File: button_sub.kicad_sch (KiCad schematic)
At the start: 6 parts, among them U3 LTV-817M

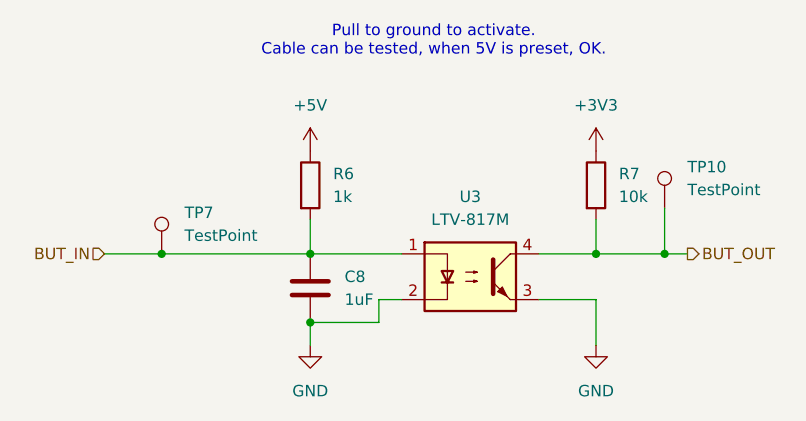
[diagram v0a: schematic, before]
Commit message: Place opto couplers and some connectors.
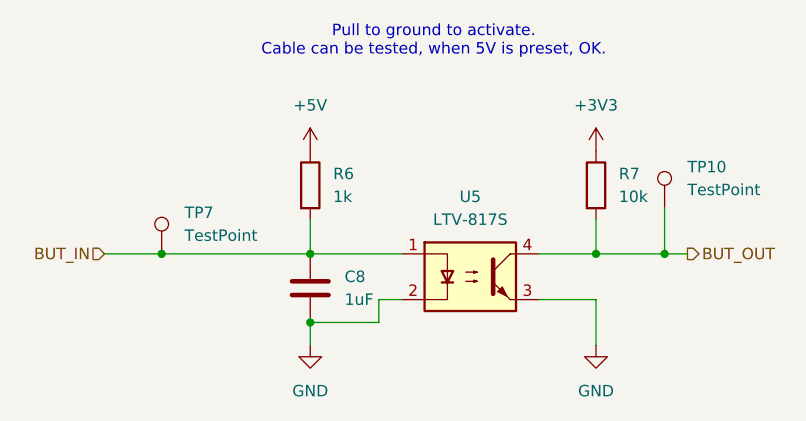
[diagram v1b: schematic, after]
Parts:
- removed U3: LTV-817M, Package_DIP:DIP-4_W10.16mm, symbol Isolator:LTV-817M
- added U5: LTV-817S, Package_DIP:SMDIP-4_W9.53mm, symbol Isolator:LTV-817S
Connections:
- net BUT_IN: now also U5.1
- net BUT_OUT: now also U5.4
- net GND: now also U5.2, U5.3
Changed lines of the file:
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@@
+	)
+	(symbol
+		(lib_id "Isolator:LTV-817S")
+		(at 151.13 99.06 0)
+		(unit 1)
+		(exclude_from_sim no)
+		(in_bom yes)
+		(on_board yes)
+		(dnp no)
+		(fields_autoplaced yes)
+		(property "Reference" "U5"
+			(at 151.13 90.17 0)
+			(effects
+				(font
+					(size 1.27 1.27)
+				)
+			)
+		)
+		(property "Value" "LTV-817S"
+			(at 151.13 92.71 0)
+			(effects
+				(font
+					(size 1.27 1.27)
+				)
+			)
+		)
+		(property "Footprint" "Package_DIP:SMDIP-4_W9.53mm"
+			(at 151.13 106.68 0)
+			(effects
+				(font
+					(size 1.27 1.27)
+				)
+				(hide yes)
+			)
+		)
+		(property "Datasheet" "https://www.lcsc.com/product-detail/C109227.html"
+			(at 142.24 91.44 0)
+			(effects
+				(font
+					(size 1.27 1.27)
+				)
+				(hide yes)
+			)
+		)
+		(property "Description" "DC Optocoupler, Vce 35V, CTR 50%, SMDIP-4"
+			(at 151.13 99.06 0)
+			(effects
+				(font
+					(size 1.27 1.27)
+				)
+				(hide yes)
+			)
+		)
+		(property "LCSC" "C109227"
+			(at 151.13 99.06 0)
+			(effects
+				(font
+					(size 1.27 1.27)
+				)
+				(hide yes)
+			)
+		)
+		(pin "4"
+		)
+		(pin "2"
+		)
+		(pin "3"
+		)
+		(pin "1"
+		)
+		(instances
+			(project ""
+				(path "/4ab90003-ea4c-4878-8117-f834ac24f8d9/2279bf67-9a91-44f0-b5c7-36e7b6560aca/1b213c25-d2ee-4039-b440-713ca9411fa9"
+					(reference "U5")
+					(unit 1)
+				)
+				(path "/4ab90003-ea4c-4878-8117-f834ac24f8d9/2279bf67-9a91-44f0-b5c7-36e7b6560aca/966e223a-98da-4719-87d2-fe9fc7de1219"
+					(reference "U6")
+					(unit 1)
+				)
+				(path "/4ab90003-ea4c-4878-8117-f834ac24f8d9/2279bf67-9a91-44f0-b5c7-36e7b6560aca/fcd7be72-9c9e-4717-8056-7ec02dc0e81d"
+					(reference "U7")
+					(unit 1)
+				)
+			)
+		)
 	)
 	(symbol
@@
 					(unit 1)
 				)
-			)
-		)
-	)
-	(symbol
-		(lib_id "Isolator:LTV-817M")
-		(at 151.13 99.06 0)
-		(unit 1)
-		(exclude_from_sim no)
-		(in_bom yes)
-		(on_board yes)
-		(dnp no)
-		(fields_autoplaced yes)
-		(property "Reference" "U3"
-			(at 151.13 90.17 0)
-			(effects
-				(font
-					(size 1.27 1.27)
-				)
-			)
-		)
-		(property "Value" "LTV-817M"
-			(at 151.13 92.71 0)
-			(effects
-				(font
-					(size 1.27 1.27)
-				)
-			)
-		)
-		(property "Footprint" "Package_DIP:DIP-4_W10.16mm"
-			(at 151.13 106.68 0)
-			(effects
-				(font
-					(size 1.27 1.27)
-				)
-				(hide yes)
-			)
-		)
-		(property "Datasheet" "https://jlcpcb.com/partdetail/LiteOn-LTV_817S_TA1C/C109227"
-			(at 140.97 91.44 0)
-			(effects
-				(font
-					(size 1.27 1.27)
-				)
-				(hide yes)
-			)
-		)
-		(property "Description" "DC Optocoupler, Vce 35V, CTR 50%, DIP-4"
-			(at 151.13 99.06 0)
-			(effects
-				(font
-					(size 1.27 1.27)
-				)
-				(hide yes)
-			)
-		)
-		(property "LCSC" "C109227"
-			(at 151.13 99.06 0)
-			(effects
-				(font
-					(size 1.27 1.27)
-				)
-				(hide yes)
-			)
-		)
-		(pin "4"
-		)
-		(pin "2"
-		)
-		(pin "3"
-		)
-		(pin "1"
-		)
-		(instances
-			(project "stopnu-hardware"
-				(path "/4ab90003-ea4c-4878-8117-f834ac24f8d9/2279bf67-9a91-44f0-b5c7-36e7b6560aca/1b213c25-d2ee-4039-b440-713ca9411fa9"
-					(reference "U3")
-					(unit 1)
-				)
-				(path "/4ab90003-ea4c-4878-8117-f834ac24f8d9/2279bf67-9a91-44f0-b5c7-36e7b6560aca/966e223a-98da-4719-87d2-fe9fc7de1219"
-					(reference "U4")
-					(unit 1)
-				)
-				(path "/4ab90003-ea4c-4878-8117-f834ac24f8d9/2279bf67-9a91-44f0-b5c7-36e7b6560aca/fcd7be72-9c9e-4717-8056-7ec02dc0e81d"
-					(reference "U2")
-					(unit 1)
-				)

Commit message: Labeled expansion port, fixed en pin U19 (high)
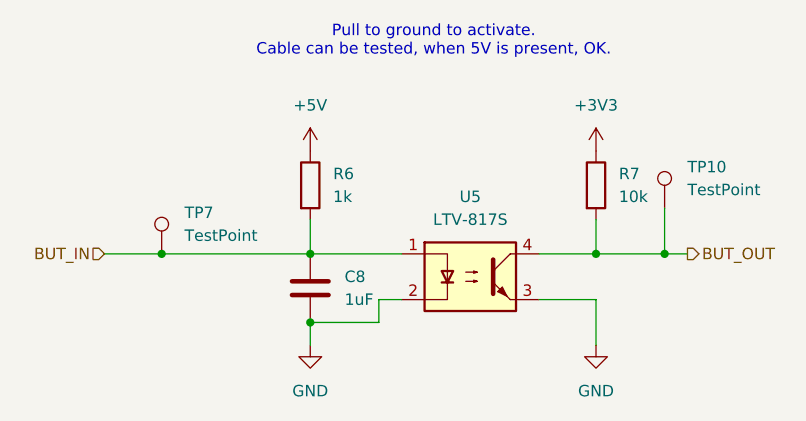
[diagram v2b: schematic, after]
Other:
- note added: "Pull to ground to activate. Cable can be tested, when 5V is present, OK."
- note removed: "Pull to ground to activate. Cable can be tested, when 5V is preset, OK."
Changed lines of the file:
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@@
 	(generator_version "9.0")
 	(paper "A4")
-	(text "Pull to ground to activate.\nCable can be tested, when 5V is preset, OK."
+	(text "Pull to ground to activate.\nCable can be tested, when 5V is present, OK."
 		(exclude_from_sim no)
 		(at 147.066 72.898 0)

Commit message: Add README.md, make power input more intuitive in schematic.
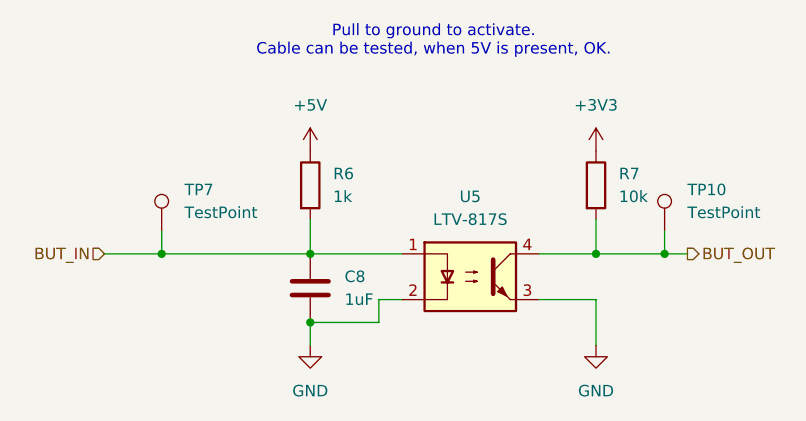
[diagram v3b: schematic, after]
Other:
- moved on the sheet: TP10, TP7
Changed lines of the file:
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@@
+	(wire
+		(pts
+			(xy 116.84 93.98) (xy 116.84 96.52)
+		)
+		(stroke
+			(width 0)
+			(type default)
+		)
+	)
 	(wire
 		(pts
@@
 	(wire
 		(pts
-			(xy 172.72 91.44) (xy 172.72 96.52)
-		)
-		(stroke
-			(width 0)
-			(type default)
-		)
-	)
-	(wire
-		(pts
 			(xy 133.35 96.52) (xy 143.51 96.52)
 		)
@@
 		(pts
 			(xy 133.35 104.14) (xy 133.35 106.68)
+		)
+		(stroke
+			(width 0)
+			(type default)
+		)
+	)
+	(wire
+		(pts
+			(xy 172.72 93.98) (xy 172.72 96.52)
 		)
 		(stroke
@@
 	(symbol
 		(lib_id "Connector:TestPoint")
-		(at 116.84 96.52 0)
+		(at 116.84 93.98 0)
 		(unit 1)
 		(exclude_from_sim no)
@@
 		(fields_autoplaced yes)
 		(property "Reference" "TP7"
+			(at 119.38 89.4079 0)
+			(effects
+				(font
+					(size 1.27 1.27)
+				)
+				(justify left)
+			)
+		)
+		(property "Value" "TestPoint"
 			(at 119.38 91.9479 0)
 			(effects
@@
 			)
 		)
-		(property "Value" "TestPoint"
-			(at 119.38 94.4879 0)
-			(effects
-				(font
-					(size 1.27 1.27)
-				)
-				(justify left)
-			)
-		)
 		(property "Footprint" "TestPoint:TestPoint_Pad_D1.0mm"
-			(at 121.92 96.52 0)
+			(at 121.92 93.98 0)
 			(effects
 				(font
@@
 		)
 		(property "Datasheet" "~"
-			(at 121.92 96.52 0)
+			(at 121.92 93.98 0)
 			(effects
 				(font
@@
 		)
 		(property "Description" "test point"
-			(at 116.84 96.52 0)
+			(at 116.84 93.98 0)
 			(effects
 				(font
@@
 	(symbol
 		(lib_id "Connector:TestPoint")
-		(at 172.72 91.44 0)
+		(at 172.72 93.98 0)
 		(unit 1)
 		(exclude_from_sim no)
@@
 		(fields_autoplaced yes)
 		(property "Reference" "TP10"
-			(at 175.26 86.8679 0)
+			(at 175.26 89.4079 0)
 			(effects
 				(font
@@
 		)
 		(property "Value" "TestPoint"
-			(at 175.26 89.4079 0)
+			(at 175.26 91.9479 0)
 			(effects
 				(font
@@
 		)
 		(property "Footprint" "TestPoint:TestPoint_Pad_D1.0mm"
-			(at 177.8 91.44 0)
+			(at 177.8 93.98 0)
 			(effects
 				(font
@@
 		)
 		(property "Datasheet" "~"
-			(at 177.8 91.44 0)
+			(at 177.8 93.98 0)
 			(effects
 				(font
@@
 		)
 		(property "Description" "test point"
-			(at 172.72 91.44 0)
-			(effects
-				(font
+			(at 172.72 93.98 0)
+			(effects
+				(font

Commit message: Fixed fabrication files, so PCBA will work with the correct rotation of the components.
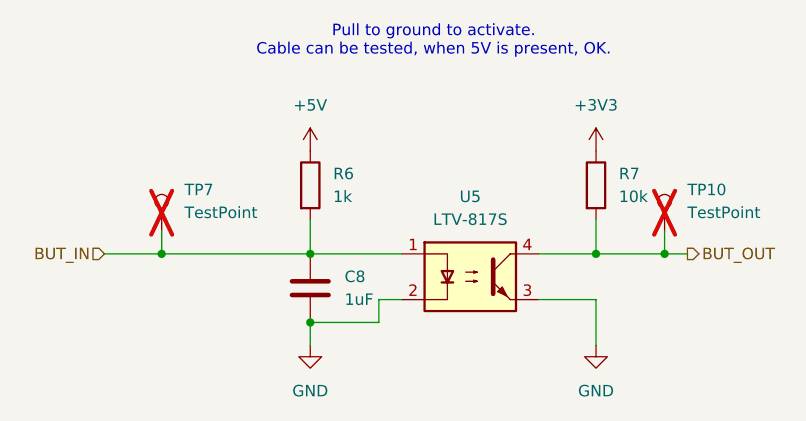
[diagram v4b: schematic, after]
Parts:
- TP10, TP7: now not fitted; now left out of the parts list
- U5: Rotation Offset (none) -> 270
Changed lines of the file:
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@@
 		(unit 1)
 		(exclude_from_sim no)
-		(in_bom yes)
+		(in_bom no)
 		(on_board yes)
-		(dnp no)
+		(dnp yes)
 		(fields_autoplaced yes)
 		(property "Reference" "TP7"
@@
 		)
 		(property "Description" "test point"
+			(at 116.84 93.98 0)
+			(effects
+				(font
+					(size 1.27 1.27)
+				)
+				(hide yes)
+			)
+		)
+		(property "gnd" ""
+			(at 116.84 93.98 0)
+			(effects
+				(font
+					(size 1.27 1.27)
+				)
+				(hide yes)
+			)
+		)
+		(property "input1" ""
+			(at 116.84 93.98 0)
+			(effects
+				(font
+					(size 1.27 1.27)
+				)
+				(hide yes)
+			)
+		)
+		(property "input2" ""
+			(at 116.84 93.98 0)
+			(effects
+				(font
+					(size 1.27 1.27)
+				)
+				(hide yes)
+			)
+		)
+		(property "input3" ""
 			(at 116.84 93.98 0)
 			(effects
@@
 			)
 		)
+		(property "gnd" ""
+			(at 165.1 88.9 0)
+			(effects
+				(font
+					(size 1.27 1.27)
+				)
+				(hide yes)
+			)
+		)
+		(property "input1" ""
+			(at 165.1 88.9 0)
+			(effects
+				(font
+					(size 1.27 1.27)
+				)
+				(hide yes)
+			)
+		)
+		(property "input2" ""
+			(at 165.1 88.9 0)
+			(effects
+				(font
+					(size 1.27 1.27)
+				)
+				(hide yes)
+			)
+		)
+		(property "input3" ""
+			(at 165.1 88.9 0)
+			(effects
+				(font
+					(size 1.27 1.27)
+				)
+				(hide yes)
+			)
+		)
 		(pin "2"
 		)
@@
 			)
 		)
+		(property "gnd" ""
+			(at 133.35 100.33 0)
+			(effects
+				(font
+					(size 1.27 1.27)
+				)
+				(hide yes)
+			)
+		)
+		(property "input1" ""
+			(at 133.35 100.33 0)
+			(effects
+				(font
+					(size 1.27 1.27)
+				)
+				(hide yes)
+			)
+		)
+		(property "input2" ""
+			(at 133.35 100.33 0)
+			(effects
+				(font
+					(size 1.27 1.27)
+				)
+				(hide yes)
+			)
+		)
+		(property "input3" ""
+			(at 133.35 100.33 0)
+			(effects
+				(font
+					(size 1.27 1.27)
+				)
+				(hide yes)
+			)
+		)
 		(pin "1"
 		)
@@
 			)
 		)
+		(property "gnd" ""
+			(at 151.13 99.06 0)
+			(effects
+				(font
+					(size 1.27 1.27)
+				)
+				(hide yes)
+			)
+		)
+		(property "input1" ""
+			(at 151.13 99.06 0)
+			(effects
+				(font
+					(size 1.27 1.27)
+				)
+				(hide yes)
+			)
+		)
+		(property "input2" ""
+			(at 151.13 99.06 0)
+			(effects
+				(font
+					(size 1.27 1.27)
+				)
+				(hide yes)
+			)
+		)
+		(property "input3" ""
+			(at 151.13 99.06 0)
+			(effects
+				(font
+					(size 1.27 1.27)
+				)
+				(hide yes)
+			)
+		)
+		(property "Rotation Offset" "270"
+			(at 151.13 99.06 0)
+			(effects
+				(font
+					(size 1.27 1.27)
+				)
+				(hide yes)
+			)
+		)
 		(pin "4"
 		)
@@
 		(unit 1)
 		(exclude_from_sim no)
-		(in_bom yes)
+		(in_bom no)
 		(on_board yes)
-		(dnp no)
+		(dnp yes)
 		(fields_autoplaced yes)
 		(property "Reference" "TP10"
@@
 		)
 		(property "Description" "test point"
+			(at 172.72 93.98 0)
+			(effects
+				(font
+					(size 1.27 1.27)
+				)
+				(hide yes)
+			)
+		)
+		(property "gnd" ""
+			(at 172.72 93.98 0)
+			(effects
+				(font
+					(size 1.27 1.27)
+				)
+				(hide yes)
+			)
+		)
+		(property "input1" ""
+			(at 172.72 93.98 0)
+			(effects
+				(font
+					(size 1.27 1.27)
+				)
+				(hide yes)
+			)
+		)
+		(property "input2" ""
+			(at 172.72 93.98 0)
+			(effects
+				(font
+					(size 1.27 1.27)
+				)
+				(hide yes)
+			)
+		)
+		(property "input3" ""
 			(at 172.72 93.98 0)
 			(effects
@@
 			(at 133.35 88.9 0)
 			(effects
+				(font
+					(size 1.27 1.27)
+				)
+				(hide yes)
+			)
+		)
+		(property "gnd" ""
+			(at 133.35 88.9 0)
+			(effects
+				(font
+					(size 1.27 1.27)
+				)
+				(hide yes)
+			)
+		)
+		(property "input1" ""
+			(at 133.35 88.9 0)
+			(effects
+				(font
+					(size 1.27 1.27)
+				)
+				(hide yes)
+			)
+		)
+		(property "input2" ""
+			(at 133.35 88.9 0)
+			(effects
+				(font
+					(size 1.27 1.27)
+				)
+				(hide yes)
+			)
+		)
+		(property "input3" ""
+			(at 133.35 88.9 0)
+			(effects
